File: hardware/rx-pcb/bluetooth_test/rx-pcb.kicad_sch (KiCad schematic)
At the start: 39 parts, among them J1 Conn_01x05_Pin, J2 Conn_01x04_Pin, J3 Conn_Coaxial_Small, J4 Conn_01x04_Pin, J5 Conn_01x02_Pin, SW1 SW_SPST, U1 STM32WB05KZV6TR, U2 STS4L-AD1B-R3, U3 STS4L-AD1B-R3, X1 Q22FA12800025, X2 ABS07-32.768KHZ-1-T

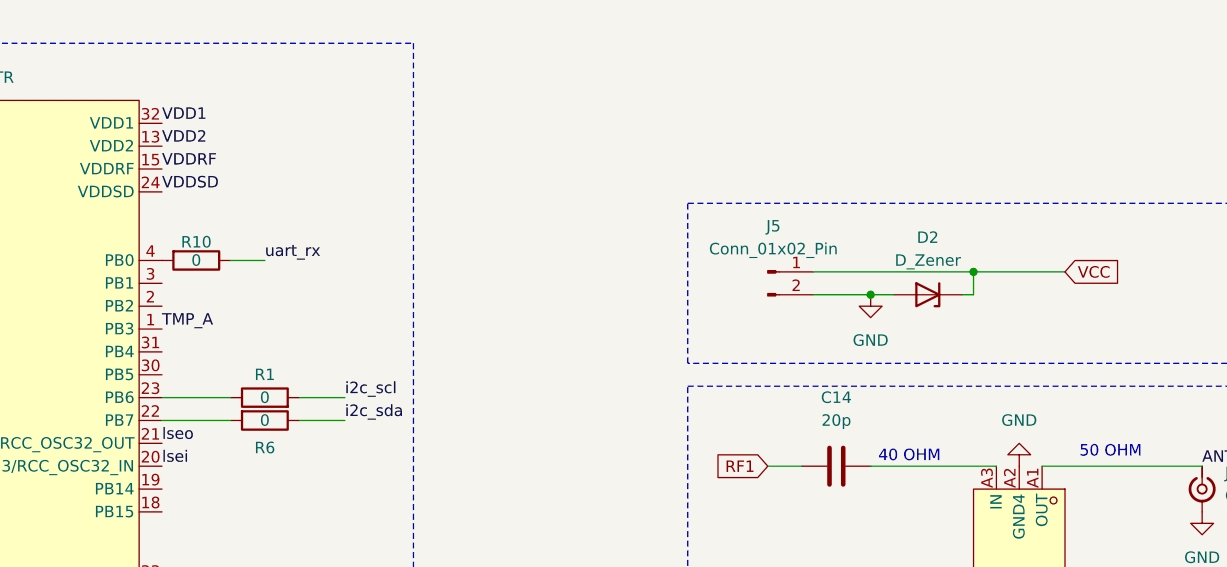
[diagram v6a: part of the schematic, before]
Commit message: updated PCB for weeks purchase
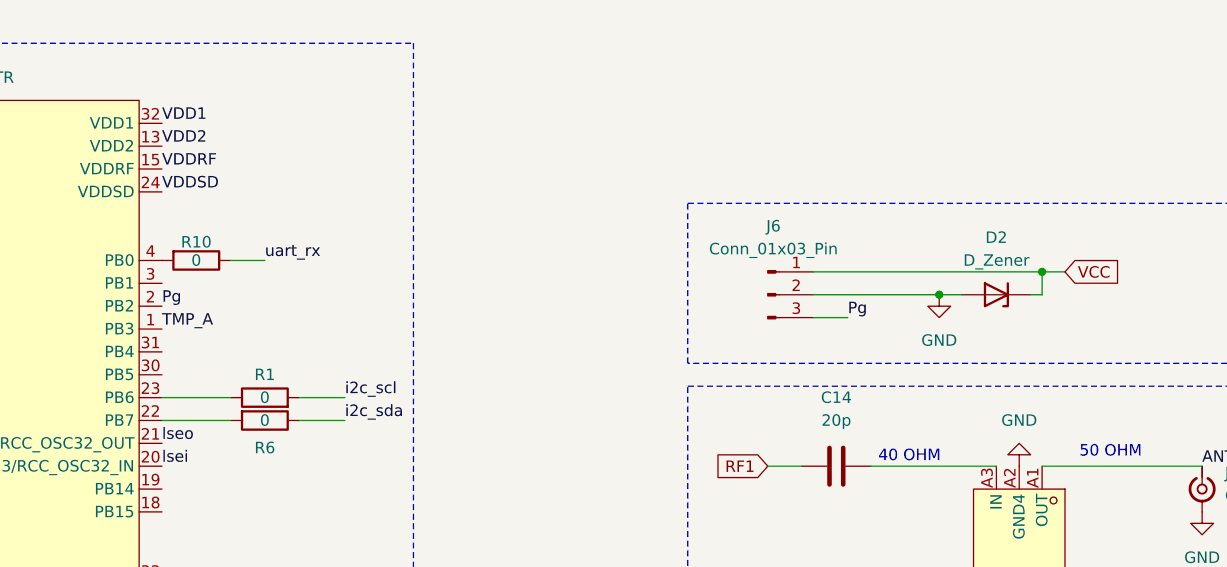
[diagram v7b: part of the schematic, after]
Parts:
- removed J5: Conn_01x02_Pin, Connector_PinHeader_2.54mm:PinHeader_1x02_P2.54mm_Vertical, symbol Connector:Conn_01x02_Pin
- added J6: Conn_01x03_Pin, Connector_PinHeader_2.54mm:PinHeader_1x03_P2.54mm_Vertical, symbol Connector:Conn_01x03_Pin
- C14: footprint Capacitor_SMD:C_0201_0603Metric_Pad0.64x0.40mm_HandSolder -> rx-parts:R_0201_0603Metric_Pad0.64x0.40mm_HandSolder_correctedclearance
- R10, R7, R8, R9: footprint Resistor_SMD:R_0201_0603Metric_Pad0.64x0.40mm_HandSolder -> Resistor_SMD:R_0805_2012Metric
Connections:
- net GND: now also J6.2 (Pin_2)
- net VCC: now also J6.1 (Pin_1)
- net Pg: now reaches U1.2 (PB2)
- net Pg: now also J6.3 (Pin_3)
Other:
- moved on the sheet: D2
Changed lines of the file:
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@@
 	)
 	(junction
-		(at 227.33 109.22)
+		(at 234.95 109.22)
 		(diameter 0)
 		(color 0 0 0 0)
@@
 	)
 	(junction
-		(at 215.9 111.76)
+		(at 223.52 111.76)
 		(diameter 0)
 		(color 0 0 0 0)
@@
 	(wire
 		(pts
-			(xy 226.06 111.76) (xy 227.33 111.76)
+			(xy 233.68 111.76) (xy 234.95 111.76)
 		)
 		(stroke
@@
 	(wire
 		(pts
-			(xy 209.55 111.76) (xy 215.9 111.76)
+			(xy 209.55 111.76) (xy 223.52 111.76)
 		)
 		(stroke
@@
 	(wire
 		(pts
-			(xy 91.44 29.21) (xy 87.63 29.21)
+			(xy 209.55 114.3) (xy 213.36 114.3)
 		)
 		(stroke
@@
 	(wire
 		(pts
-			(xy 46.99 109.22) (xy 40.64 109.22)
+			(xy 91.44 29.21) (xy 87.63 29.21)
 		)
 		(stroke
@@
 	(wire
 		(pts
-			(xy 227.33 109.22) (xy 237.49 109.22)
+			(xy 46.99 109.22) (xy 40.64 109.22)
 		)
 		(stroke
@@
 	(wire
 		(pts
-			(xy 227.33 111.76) (xy 227.33 109.22)
+			(xy 234.95 111.76) (xy 234.95 109.22)
 		)
 		(stroke
@@
 	(wire
 		(pts
+			(xy 234.95 109.22) (xy 237.49 109.22)
+		)
+		(stroke
+			(width 0)
+			(type default)
+		)
+	)
+	(wire
+		(pts
 			(xy 134.62 35.56) (xy 133.35 35.56)
 		)
@@
 	(wire
 		(pts
-			(xy 215.9 111.76) (xy 218.44 111.76)
+			(xy 223.52 111.76) (xy 226.06 111.76)
 		)
 		(stroke
@@
 	(wire
 		(pts
-			(xy 209.55 109.22) (xy 227.33 109.22)
+			(xy 209.55 109.22) (xy 234.95 109.22)
 		)
 		(stroke
@@
 		)
 	)
+	(label "Pg"
+		(at 137.16 113.03 0)
+		(effects
+			(font
+				(size 1.27 1.27)
+			)
+			(justify left bottom)
+		)
+	)
 	(label "VCAP"
 		(at 38.1 142.24 0)
@@
 		)
 	)
+	(label "Pg"
+		(at 213.36 114.3 0)
+		(effects
+			(font
+				(size 1.27 1.27)
+			)
+			(justify left bottom)
+		)
+	)
 	(label "vlxsd"
 		(at 43.18 58.42 0)
@@
 			)
 		)
-		(property "Footprint" "Resistor_SMD:R_0201_0603Metric_Pad0.64x0.40mm_HandSolder"
+		(property "Footprint" "Resistor_SMD:R_0805_2012Metric"
 			(at 80.01 132.842 90)
 			(hide yes)
@@
 			)
 		)
-		(property "Footprint" "Capacitor_SMD:C_0201_0603Metric_Pad0.64x0.40mm_HandSolder"
+		(property "Footprint" "rx-parts:R_0201_0603Metric_Pad0.64x0.40mm_HandSolder_correctedclearance"
 			(at 215.9 129.8448 0)
 			(hide yes)
@@
 			)
 		)
-		(property "Footprint" "Resistor_SMD:R_0201_0603Metric_Pad0.64x0.40mm_HandSolder"
+		(property "Footprint" "Resistor_SMD:R_0805_2012Metric"
 			(at 80.01 130.302 90)
 			(hide yes)
@@
 			)
 		)
-		(property "Footprint" "Resistor_SMD:R_0201_0603Metric_Pad0.64x0.40mm_HandSolder"
+		(property "Footprint" "Resistor_SMD:R_0805_2012Metric"
 			(at 80.01 131.318 90)
 			(hide yes)
@@
 	(symbol
 		(lib_id "rx-parts:GND")
-		(at 215.9 111.76 0)
+		(at 223.52 111.76 0)
 		(unit 1)
 		(body_style 1)
@@
 		(fields_autoplaced yes)
 		(property "Reference" "#PWR021"
-			(at 215.9 118.11 0)
+			(at 223.52 118.11 0)
 			(hide yes)
 			(show_name no)
@@
 		)
 		(property "Value" "GND"
-			(at 215.9 116.84 0)
+			(at 223.52 116.84 0)
 			(show_name no)
 			(do_not_autoplace no)
@@
 		)
 		(property "Footprint" ""
-			(at 215.9 111.76 0)
+			(at 223.52 111.76 0)
 			(hide yes)
 			(show_name no)
@@
 		)
 		(property "Datasheet" ""
-			(at 215.9 111.76 0)
+			(at 223.52 111.76 0)
 			(hide yes)
 			(show_name no)
@@
 		)
 		(property "Description" "Power symbol creates a global label with name \"GND\" , ground"
-			(at 215.9 111.76 0)
+			(at 223.52 111.76 0)
 			(hide yes)
 			(show_name no)
@@
 			)
 		)
-		(property "Footprint" "Resistor_SMD:R_0201_0603Metric_Pad0.64x0.40mm_HandSolder"
+		(property "Footprint" "Resistor_SMD:R_0805_2012Metric"
 			(at 140.97 106.172 90)
 			(hide yes)
@@
 	(symbol
 		(lib_id "Device:D_Zener")
-		(at 222.25 111.76 180)
+		(at 229.87 111.76 180)
 		(unit 1)
 		(body_style 1)
@@
 		(fields_autoplaced yes)
 		(property "Reference" "D2"
-			(at 222.25 105.41 0)
+			(at 229.87 105.41 0)
 			(show_name no)
 			(do_not_autoplace no)
@@
 		)
 		(property "Value" "D_Zener"
-			(at 222.25 107.95 0)
+			(at 229.87 107.95 0)
 			(show_name no)
 			(do_not_autoplace no)
@@
 		)
 		(property "Footprint" "Diode_SMD:D_0603_1608Metric_Pad1.05x0.95mm_HandSolder"
-			(at 222.25 111.76 0)
+			(at 229.87 111.76 0)
 			(hide yes)
 			(show_name no)
@@
 		)
 		(property "Datasheet" ""
-			(at 222.25 111.76 0)
+			(at 229.87 111.76 0)
 			(hide yes)
 			(show_name no)
@@
 		)
 		(property "Description" "Zener diode"
-			(at 222.25 111.76 0)
+			(at 229.87 111.76 0)
 			(hide yes)
 			(show_name no)
@@
 	)
 	(symbol
+		(lib_id "Connector:Conn_01x03_Pin")
+		(at 204.47 111.76 0)
+		(unit 1)
+		(body_style 1)
+		(exclude_from_sim no)
+		(in_bom yes)
+		(on_board yes)
+		(in_pos_files yes)
+		(dnp no)
+		(fields_autoplaced yes)
+		(property "Reference" "J6"
+			(at 205.105 104.14 0)
+			(show_name no)
+			(do_not_autoplace no)
+			(effects
+				(font
+					(size 1.27 1.27)
+				)
+			)
+		)
+		(property "Value" "Conn_01x03_Pin"
+			(at 205.105 106.68 0)
+			(show_name no)
+			(do_not_autoplace no)
+			(effects
+				(font
+					(size 1.27 1.27)
+				)
+			)
+		)
+		(property "Footprint" "Connector_PinHeader_2.54mm:PinHeader_1x03_P2.54mm_Vertical"
+			(at 204.47 111.76 0)
+			(hide yes)
+			(show_name no)
+			(do_not_autoplace no)
+			(effects
+				(font
+					(size 1.27 1.27)
+				)
+			)
+		)
+		(property "Datasheet" ""
+			(at 204.47 111.76 0)
+			(hide yes)
+			(show_name no)
+			(do_not_autoplace no)
+			(effects
+				(font
+					(size 1.27 1.27)
+				)
+			)
+		)
+		(property "Description" "Generic connector, single row, 01x03, script generated"
+			(at 204.47 111.76 0)
+			(hide yes)
+			(show_name no)
+			(do_not_autoplace no)
+			(effects
+				(font
+					(size 1.27 1.27)
+				)
+			)
+		)
+		(pin "1"
+		)
+		(pin "2"
+		)
+		(pin "3"
+		)
+		(instances
+			(project "rx-pcb"
+				(path "/9df8ddb8-545e-44cf-b4e7-941b19ec42ab"
+					(reference "J6")
+					(unit 1)
+				)
+			)
+		)
+	)
+	(symbol
 		(lib_id "rx-parts:GND")
 		(at 38.1 33.02 90)
@@
 					(unit 1)
 				)
-			)
-		)
-	)
-	(symbol
-		(lib_id "Connector:Conn_01x02_Pin")
-		(at 204.47 109.22 0)
-		(unit 1)
-		(body_style 1)
-		(exclude_from_sim no)
-		(in_bom yes)
-		(on_board yes)
-		(in_pos_files yes)
-		(dnp no)
-		(fields_autoplaced yes)
-		(property "Reference" "J5"
-			(at 205.105 104.14 0)
-			(show_name no)
-			(do_not_autoplace no)
-			(effects
-				(font
-					(size 1.27 1.27)
-				)
-			)
-		)
-		(property "Value" "Conn_01x02_Pin"
-			(at 205.105 106.68 0)
-			(show_name no)
-			(do_not_autoplace no)
-			(effects
-				(font
-					(size 1.27 1.27)
-				)
-			)
-		)
-		(property "Footprint" "Connector_PinHeader_2.54mm:PinHeader_1x02_P2.54mm_Vertical"
-			(at 204.47 109.22 0)
-			(hide yes)
-			(show_name no)
-			(do_not_autoplace no)
-			(effects
-				(font
-					(size 1.27 1.27)
-				)
-			)
-		)
-		(property "Datasheet" ""
-			(at 204.47 109.22 0)
-			(hide yes)
-			(show_name no)
-			(do_not_autoplace no)
-			(effects
-				(font
-					(size 1.27 1.27)
-				)
-			)
-		)
-		(property "Description" "Generic connector, single row, 01x02, script generated"
-			(at 204.47 109.22 0)
-			(hide yes)
-			(show_name no)
-			(do_not_autoplace no)
-			(effects
-				(font
-					(size 1.27 1.27)
-				)
-			)
-		)
-		(pin "2"
-		)
-		(pin "1"
-		)
-		(instances
-			(project "rx-pcb"
-				(path "/9df8ddb8-545e-44cf-b4e7-941b19ec42ab"
-					(reference "J5")
-					(unit 1)
-				)
